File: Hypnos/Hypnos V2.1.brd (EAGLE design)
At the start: 25.6 x 52 mm, 32 parts

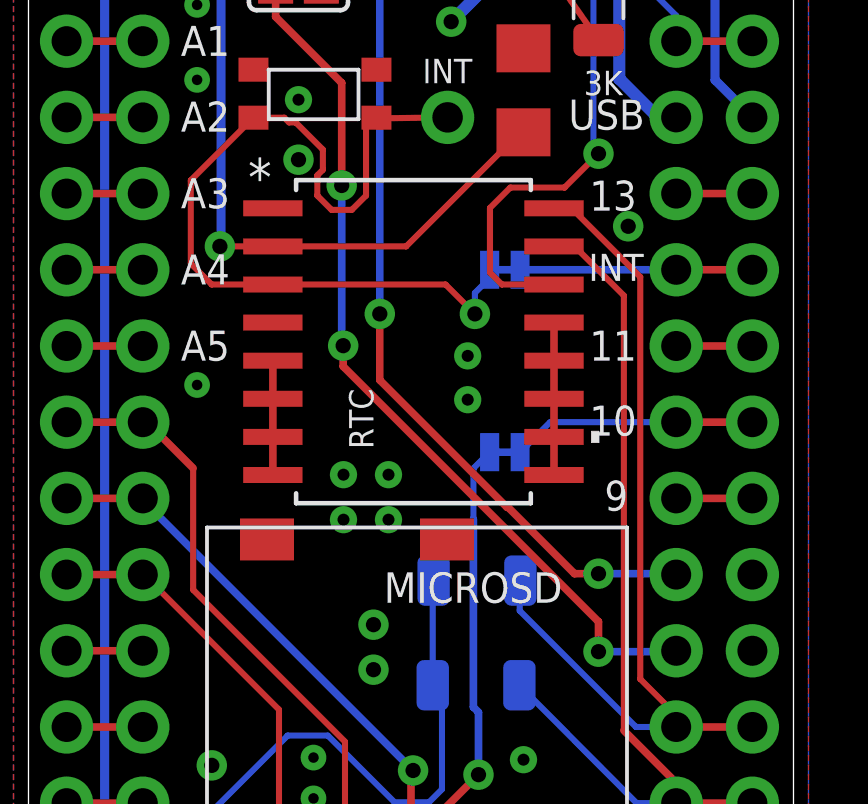
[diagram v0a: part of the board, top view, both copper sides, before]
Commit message: Update 3V trace for Hypnos V3
Route missing trace for V3
Add bStop layer for V2
Clean up some note on schematic V2 and V3
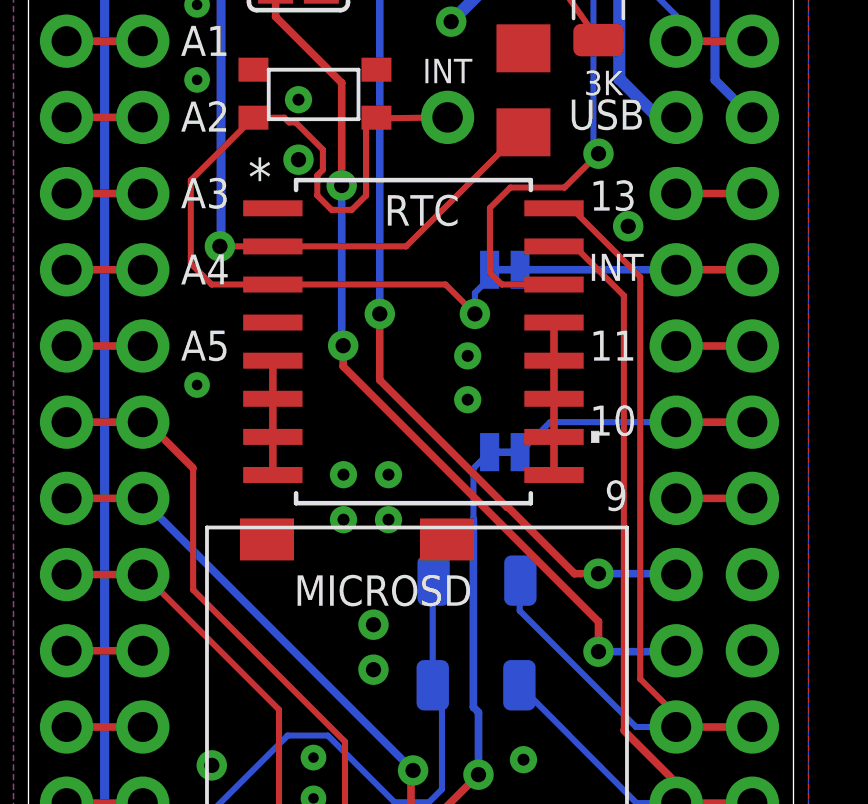
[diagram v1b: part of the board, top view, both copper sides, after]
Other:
- board text removed: "RTC"
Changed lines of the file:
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@@
 <?xml version="1.0" encoding="utf-8"?>
 <!DOCTYPE eagle SYSTEM "eagle.dtd">
-<eagle version="9.5.2">
+<eagle version="9.5.0">
 <drawing>
 <settings>
-<setting alwaysvectorfont="no"/>
+<setting alwaysvectorfont="yes"/>
 <setting verticaltext="up"/>
 </settings>
 <grid distance="0.1" unitdist="mm" unit="mm" style="lines" multiple="1" display="no" altdistance="0.01" altunitdist="mm" altunit="mm"/>
 <layers>
-<layer number="1" name="Top" color="4" fill="1" visible="no" active="yes"/>
+<layer number="1" name="Top" color="4" fill="1" visible="yes" active="yes"/>
 <layer number="2" name="Route2" color="16" fill="1" visible="no" active="no"/>
 <layer number="3" name="Route3" color="17" fill="1" visible="no" active="no"/>
@@
 <layer number="19" name="Unrouted" color="6" fill="1" visible="yes" active="yes"/>
 <layer number="20" name="Dimension" color="24" fill="1" visible="yes" active="yes"/>
-<layer number="21" name="tPlace" color="7" fill="1" visible="no" active="yes"/>
+<layer number="21" name="tPlace" color="7" fill="1" visible="yes" active="yes"/>
 <layer number="22" name="bPlace" color="7" fill="1" visible="yes" active="yes"/>
 <layer number="23" name="tOrigins" color="15" fill="1" visible="no" active="yes"/>
 <layer number="24" name="bOrigins" color="15" fill="1" visible="yes" active="yes"/>
-<layer number="25" name="tNames" color="7" fill="1" visible="no" active="yes"/>
+<layer number="25" name="tNames" color="7" fill="1" visible="yes" active="yes"/>
 <layer number="26" name="bNames" color="7" fill="1" visible="yes" active="yes"/>
 <layer number="27" name="tValues" color="7" fill="1" visible="no" active="yes"/>
@@
 <text x="23.2" y="1.6" size="0.9" layer="21" ratio="10">G</text>
 <text x="22.9" y="1.3" size="1.016" layer="22" rot="MR0">Bao Nguyen &amp; Bryson Goto</text>
-<text x="12.79" y="25.71" size="1.016" layer="22" ratio="10" rot="MR180">RTC</text>
 <wire x1="26.5" y1="50" x2="26.5" y2="49.5" width="0.0762" layer="20"/>
 <wire x1="1" y1="49" x2="1" y2="50" width="0.0762" layer="20"/>
@@
 <wire x1="2.5" y1="2.4" x2="2.5" y2="4" width="0.15" layer="21"/>
 <wire x1="4.5" y1="3.8" x2="4.5" y2="2.7" width="0.15" layer="21"/>
+<text x="20" y="4.5" size="1.4224" layer="30" ratio="15" rot="MR0">Hypnos V2.1</text>
 </plain>
 <attributes>
@@
 </element>
 <element name="MICROSD" library="adafruit" library_urn="urn:adsk.eagle:library:420" package="MICROSD" package3d_urn="urn:adsk.eagle:package:6240723/1" value="MICROSD" x="6.95" y="16.78" smashed="yes">
-<attribute name="NAME" x="12.847" y="14.229" size="1.016" layer="25" ratio="10"/>
+<attribute name="NAME" x="9.847" y="14.129" size="1.016" layer="25" ratio="10"/>
 </element>
 <element name="RTC" library="power8" package="21-0042B_16" value="DS3231ST&amp;R" x="13.832" y="22.934" smashed="yes">
 <attribute name="MANUFACTURER_PART_NUMBER" value="DS3231S#T&amp;R" x="69.712" y="-7.546" size="1.778" layer="27" display="off"/>
-<attribute name="NAME" x="12.499" y="19.3564" size="0.8128" layer="25" ratio="9" rot="SR90"/>
+<attribute name="NAME" x="12.8564" y="26.801" size="1.016" layer="25" ratio="9" rot="SR0"/>
 <attribute name="VENDOR" value="Maxim Integrated Products" x="69.712" y="-7.546" size="1.778" layer="27" display="off"/>
 </element>
